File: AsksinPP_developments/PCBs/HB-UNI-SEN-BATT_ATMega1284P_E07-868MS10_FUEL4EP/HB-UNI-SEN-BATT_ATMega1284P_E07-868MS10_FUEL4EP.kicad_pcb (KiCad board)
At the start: 2 copper layers, 75 x 75 mm, 56 parts, among them J1 Conn_01x02, J10 charge, J11 ePaper connector, J12 FTDI Debuger, J2 Conn_01x02, J3 Conn_01x02, J4 Conn_01x02, J5 ISP Programmer, J6 Conn_01x04, J7 Conn_01x04, J8 Conn_01x04, J9 Conn_01x04, Q1 IRLU024N, SW1 Config button, SW2 Reset button, U1 ATmega1284P-AU, U2 TPS61221DCK, Y1 8MHz

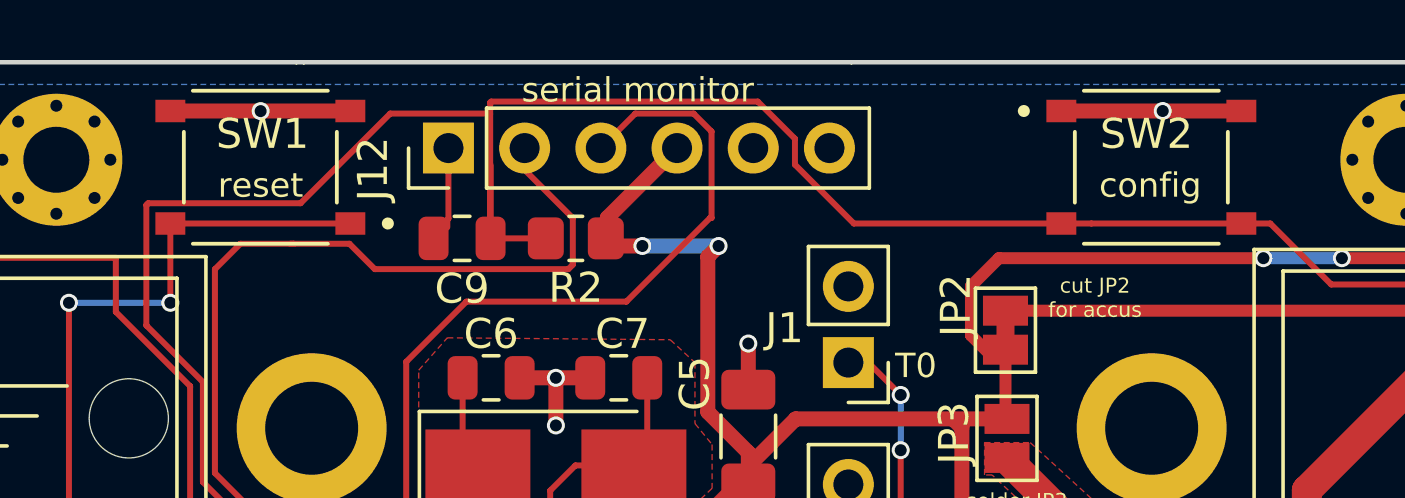
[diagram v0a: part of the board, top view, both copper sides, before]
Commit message: PCBs/HB-UNI-SEN-BATT_ATMega1284P_E07-868MS10_FUEL4EP and PCBs/HB-UNI-SEN-BATT_ATMega1284P_E07-868MS10_FRAM_FUEL4EP: changed R8 from 200kOhm to 47kOhm for better measurement accuracy
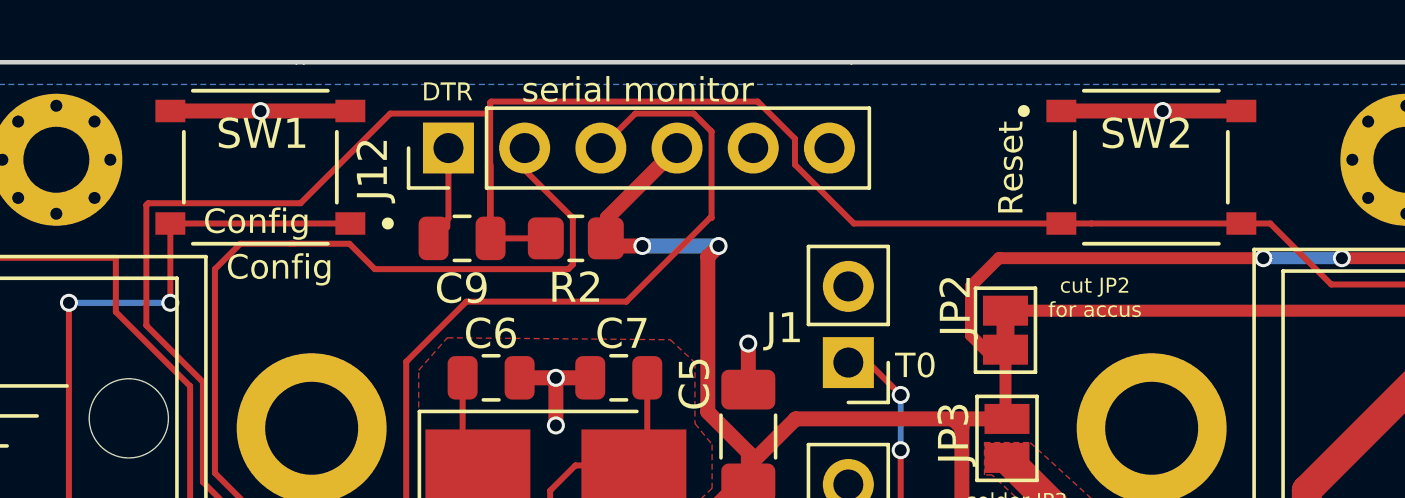
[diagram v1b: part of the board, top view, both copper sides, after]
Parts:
- R8: value 200k -> 47k
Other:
- board text added: "Config"
- board text added: "DTR"
- board text added: "Reset"
- board text added: "Version 1.1 - 01/2022"
- board text removed: "Version 1.0 - 10/2021"
- board text removed: "config"
- board text removed: "reset"

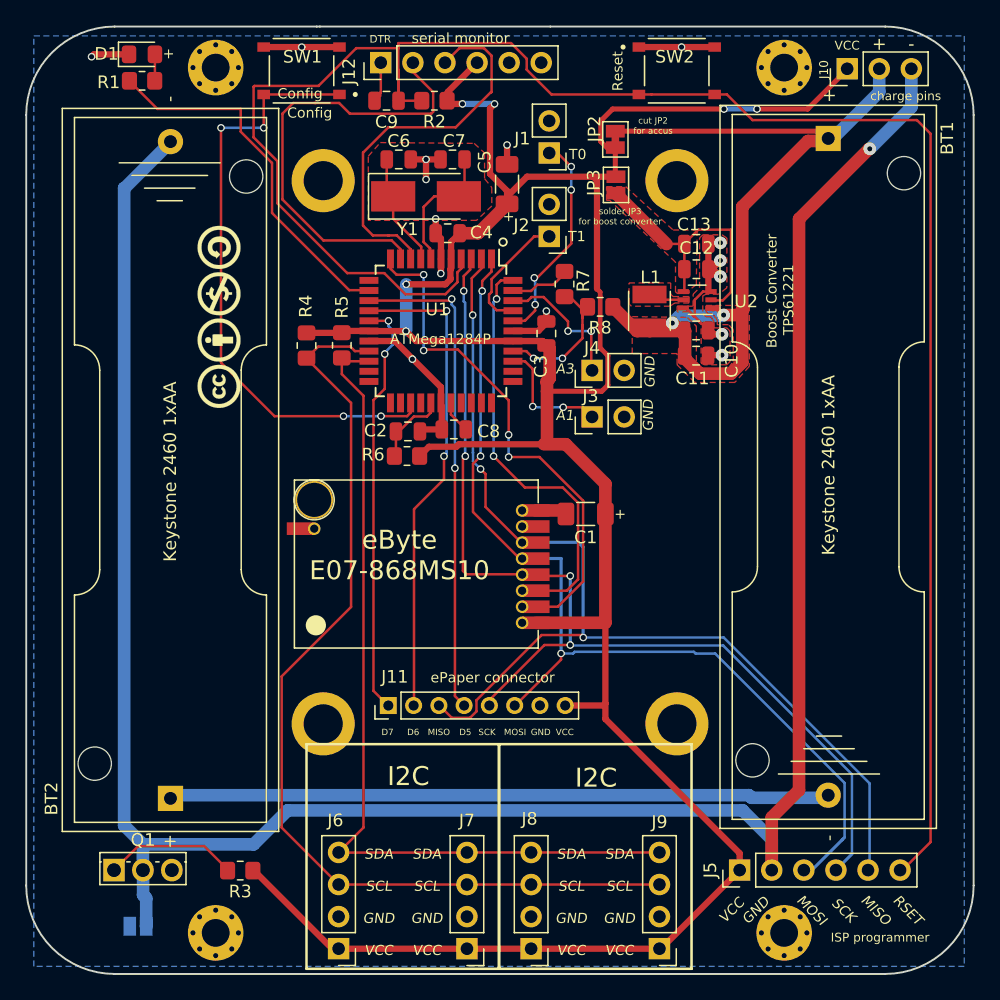
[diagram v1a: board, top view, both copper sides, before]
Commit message: major update: hb-ep-devices-addon V1.14; added sketches HB-UNI-Sensor1-AQ-BME680_KF_rLF and HB-UNI-SenAct-4-4-SC_DS; migration of all PPCBs to KiCAD 6
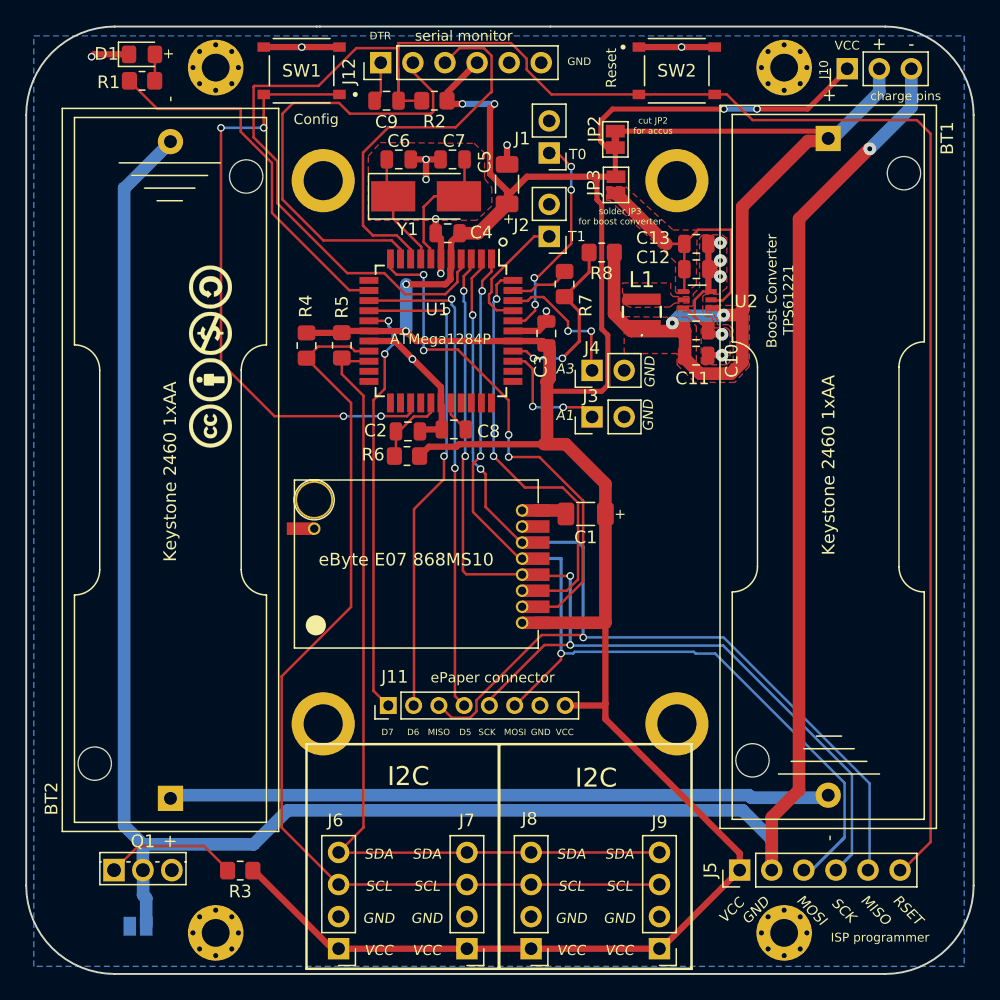
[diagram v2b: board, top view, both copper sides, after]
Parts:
- L1: footprint FUEL4EP:Fastron L-1212FPS 4.7uH SMD Inductor -> FUEL4EP:FUEL4EP_Inductor_SMD_1
- moved R8 4.30 mm to (146.6, 95.9)
- moved LOGO1 3.21 mm to (115.6, 104.1)
- moved L1 1.75 mm to (149.7, 100.6)
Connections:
- Module1 pad 2A: Net-(Module1-Pad2A) -> unconnected-(Module1-Pad2A)
- Module1 pad 7C: Net-(Module1-Pad7C) -> unconnected-(Module1-Pad7C)
- U1 pad 12: Net-(U1-Pad12) -> unconnected-(U1-Pad12)
- U1 pad 21: Net-(U1-Pad21) -> unconnected-(U1-Pad21)
- U1 pad 22: Net-(U1-Pad22) -> unconnected-(U1-Pad22)
- U1 pad 23: Net-(U1-Pad23) -> unconnected-(U1-Pad23)
- U1 pad 24: Net-(U1-Pad24) -> unconnected-(U1-Pad24)
- U1 pad 26: Net-(U1-Pad26) -> unconnected-(U1-Pad26)
- U1 pad 30: Net-(U1-Pad30) -> unconnected-(U1-Pad30)
- U1 pad 31: Net-(U1-Pad31) -> unconnected-(U1-Pad31)
- U1 pad 32: Net-(U1-Pad32) -> unconnected-(U1-Pad32)
- U1 pad 33: Net-(U1-Pad33) -> unconnected-(U1-Pad33)
- U1 pad 34: Net-(U1-Pad34) -> unconnected-(U1-Pad34)
- U1 pad 35: Net-(U1-Pad35) -> unconnected-(U1-Pad35)
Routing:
- net /plusBAT: track 69.9 -> 74.6 mm
- net VCC: track 224.0 -> 220.7 mm
- net Net-(L1-Pad2): track 2.67 -> 0.00 mm
- net /A0: track 12.1 -> 14.4 mm
- net /minusBAT: track 187.3 -> 186.7 mm
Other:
- net class Default removed
- net class battery removed
- net class supply removed
- board text added: "Version 1.2 - 07/2023 (KiCAD 6)"
- board text removed: "Version 1.1 - 01/2022"
- board text removed: "eByte E07-868MS10"

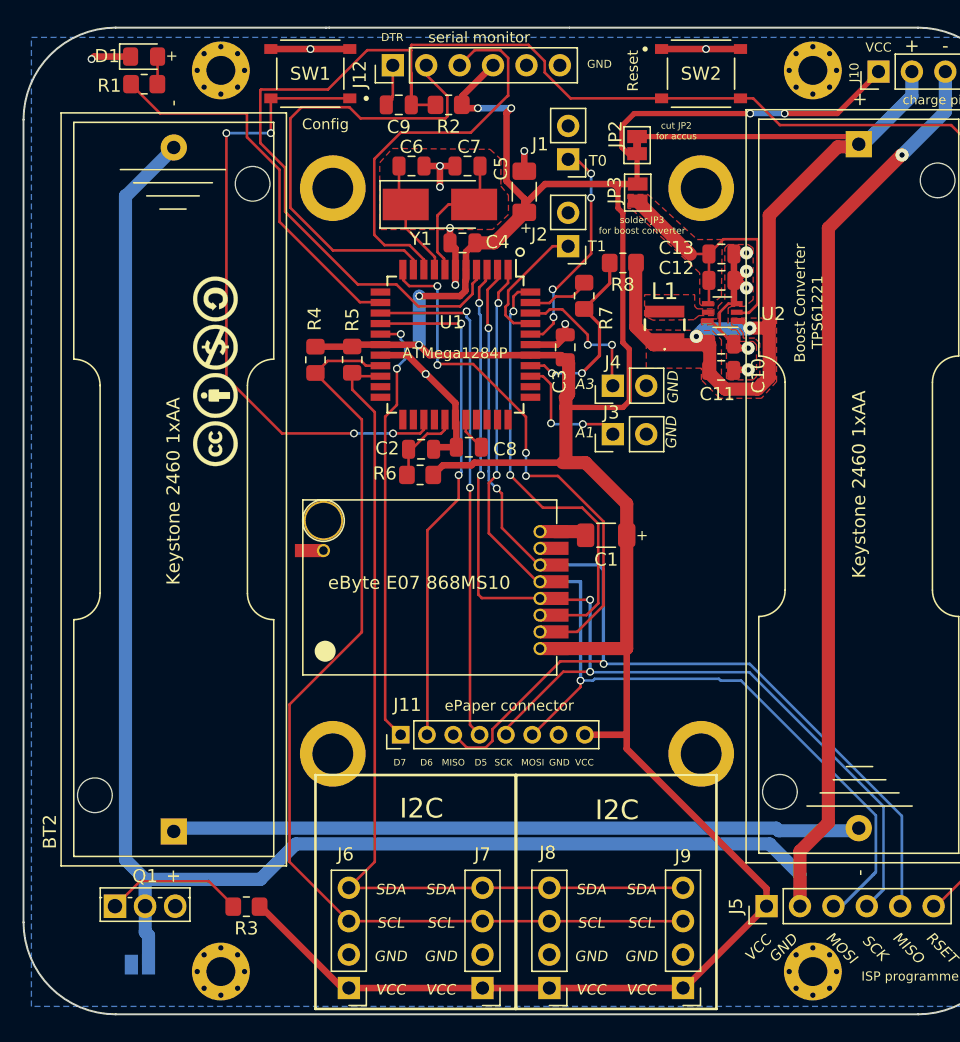
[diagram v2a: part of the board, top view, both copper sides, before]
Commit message: PCBs: KiCAD6 required improvements of layout data bases; added E07-900M10S into FUEL and footprint library
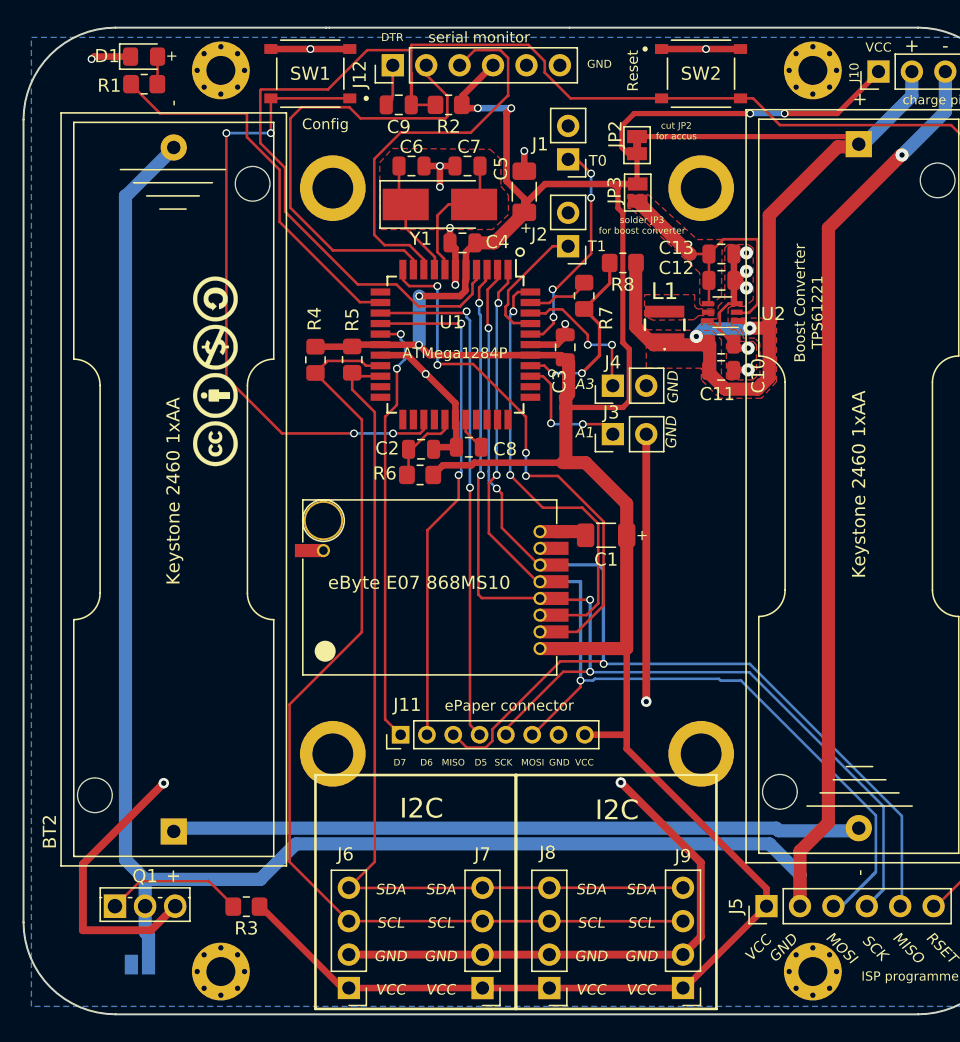
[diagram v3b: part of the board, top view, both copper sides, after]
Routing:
- net GND: track 57.4 -> 140.6 mm, vias 15 -> 18
- net /PB0_T0: track 17.5 -> 16.2 mm
- net VCC: track 220.7 -> 219.6 mm
- net /plusBAT: track 74.6 -> 73.8 mm
- net /Vout: track 21.6 -> 20.8 mm
- net /TXD0: track 35.8 -> 35.0 mm
- net /MOSI: track 79.1 -> 78.5 mm
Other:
- board text added: "Version 1.3 - 07/2023 (KiCAD 6)"
- board text removed: "Version 1.2 - 07/2023 (KiCAD 6)"

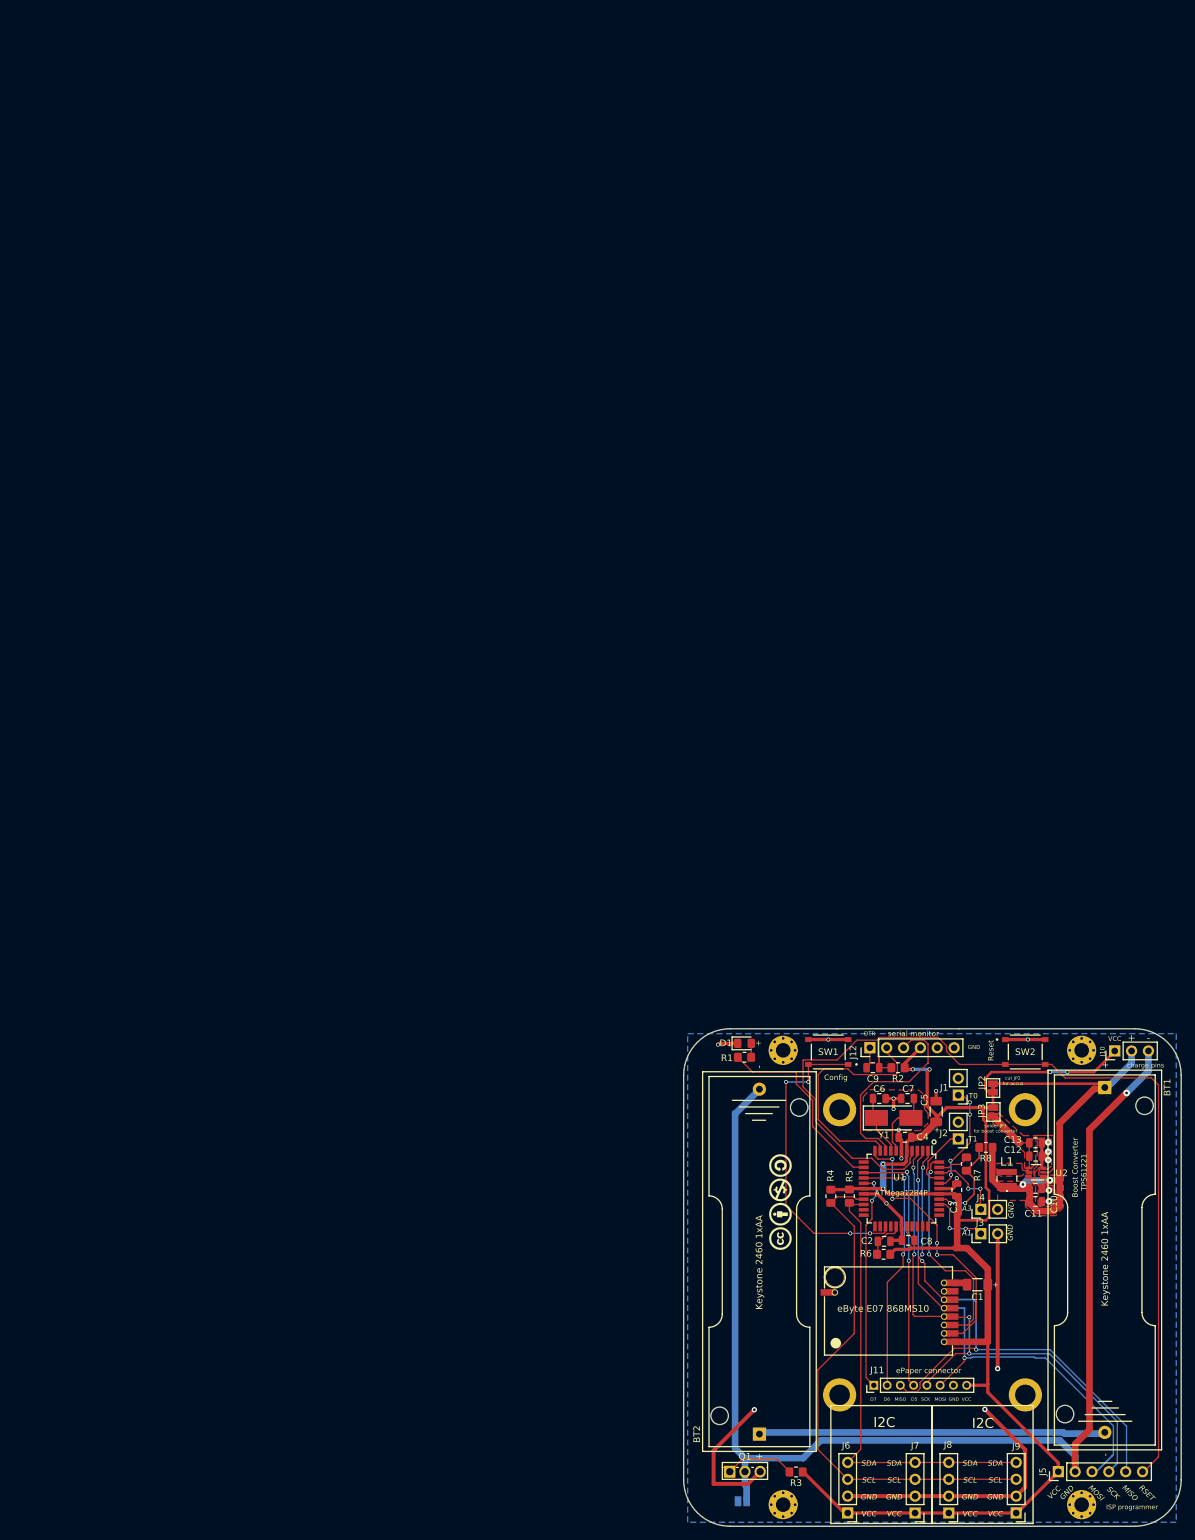
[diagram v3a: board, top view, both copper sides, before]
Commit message: PCBs: Fixes to ensure a proper production at JLCPCB, e.g. corrections of origins, rotations of assembled ICs etc.
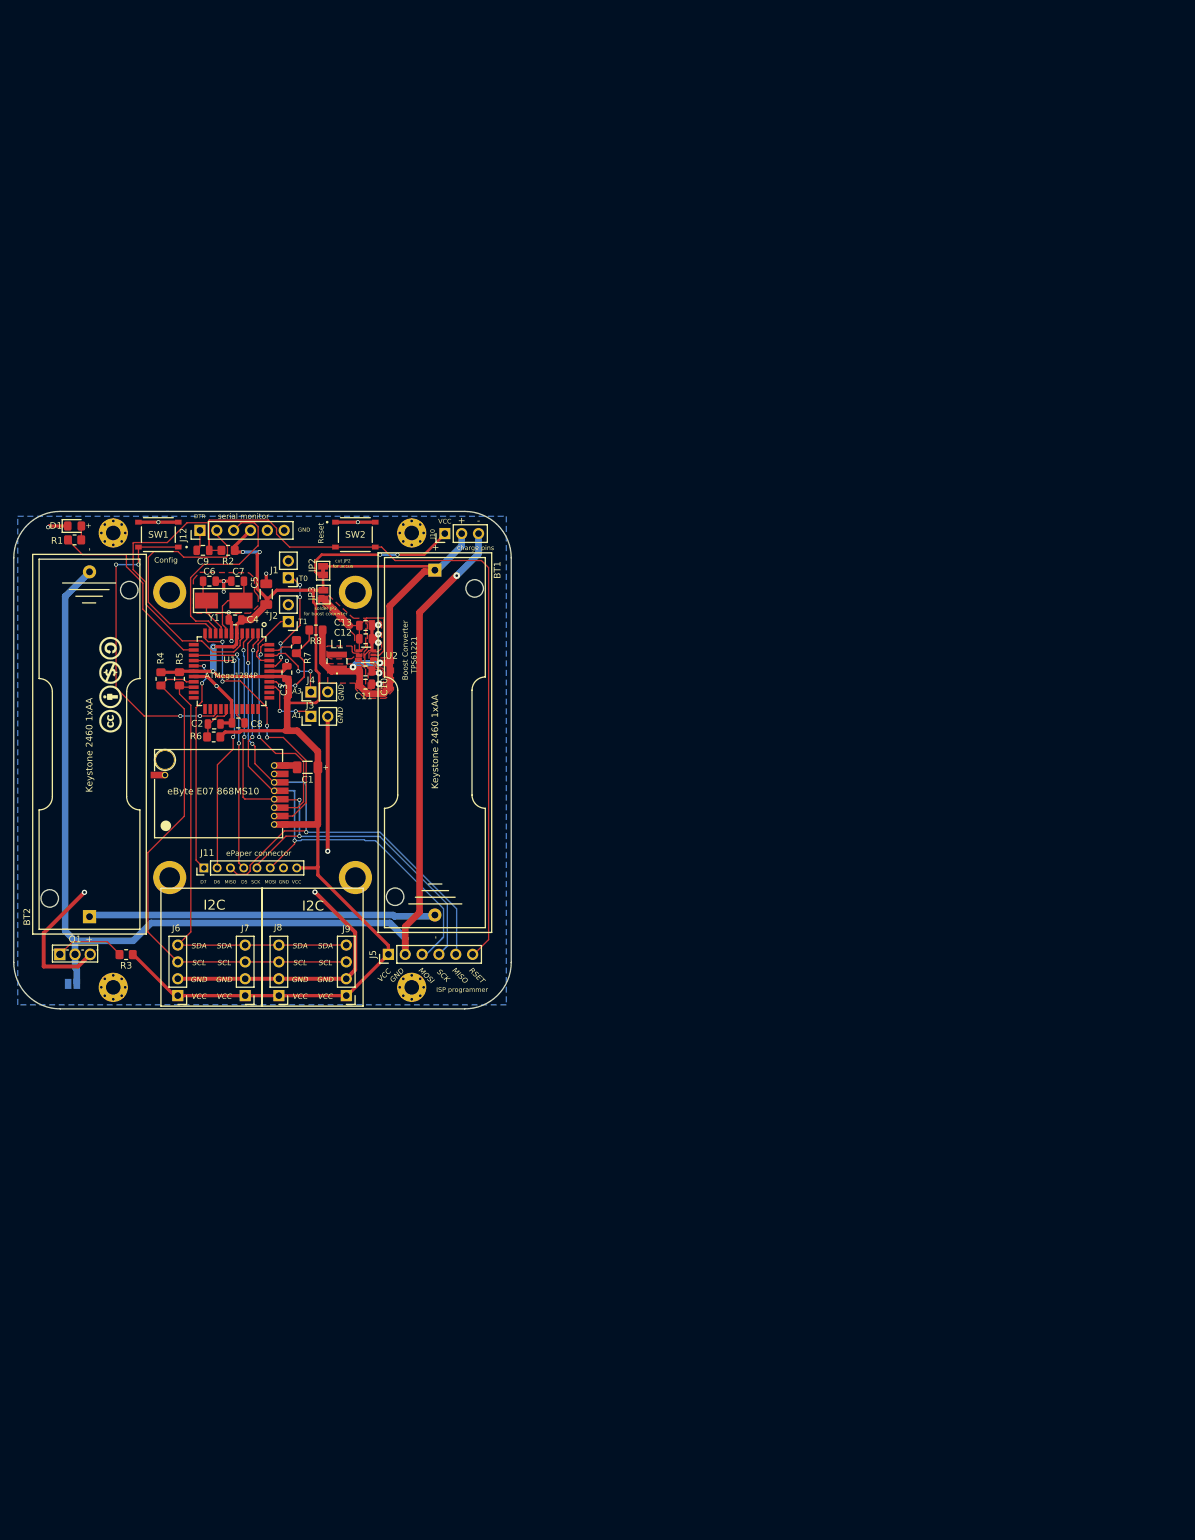
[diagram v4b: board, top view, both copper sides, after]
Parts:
- moved C1 127.6 mm to (44.3, 38.6)
- moved C4 127.6 mm to (33.4, 16.4)
- moved C7 127.6 mm to (33.7, 10.5)
- moved U1 127.6 mm to (32.8, 24.1)
- moved BT1 127.6 mm to (63.5, 8.86)
- moved BT2 127.6 mm to (11.4, 61.1)
- moved C10 127.6 mm to (53.0, 24.1)
- moved C11 127.6 mm to (53.0, 26.1)
- moved C12 127.6 mm to (53.1, 19.2)
- moved C13 127.6 mm to (53.1, 17.2)
- moved C2 127.6 mm to (30.2, 32.0)
- moved C3 127.6 mm to (41.2, 24.3)
- moved C5 127.6 mm to (38.1, 12.5)
- moved C6 127.6 mm to (29.5, 10.5)
- moved C8 127.6 mm to (33.9, 31.9)
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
